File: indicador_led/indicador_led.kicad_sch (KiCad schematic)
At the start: 3 parts, among them J1 Conn_01x02_Pin

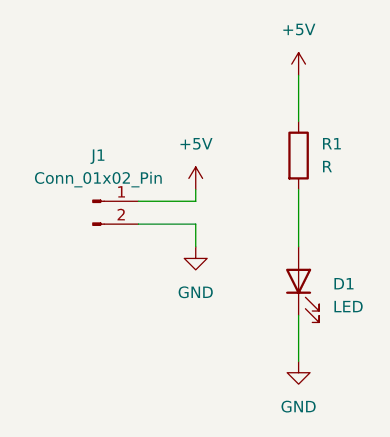
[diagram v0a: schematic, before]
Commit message: fix: altera R1 de 1k para 680 ohms
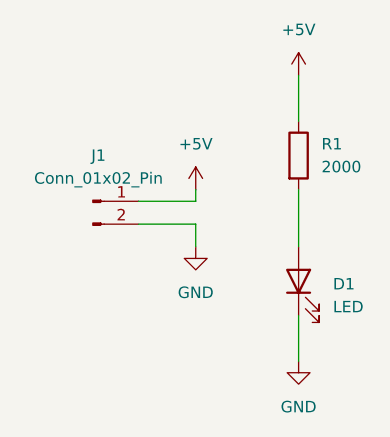
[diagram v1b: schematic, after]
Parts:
- R1: value R -> 2000
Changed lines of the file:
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@@
 			)
 		)
-		(property "Value" "R"
+		(property "Value" "2000"
 			(at 107.95 102.8699 0)
 			(show_name no)

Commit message: mudar o resistor para 1k
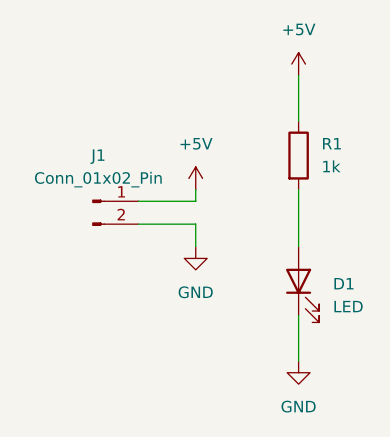
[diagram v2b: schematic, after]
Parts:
- R1: value 2000 -> 1k
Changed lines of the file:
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@@
 			)
 		)
-		(property "Value" "2000"
+		(property "Value" "1k"
 			(at 107.95 102.8699 0)
 			(show_name no)
